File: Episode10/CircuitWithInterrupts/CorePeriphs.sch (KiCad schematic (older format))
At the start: 10 parts, among them J303 Conn_01x05, U301 82C55A, U302 82C54, U303 MC6850

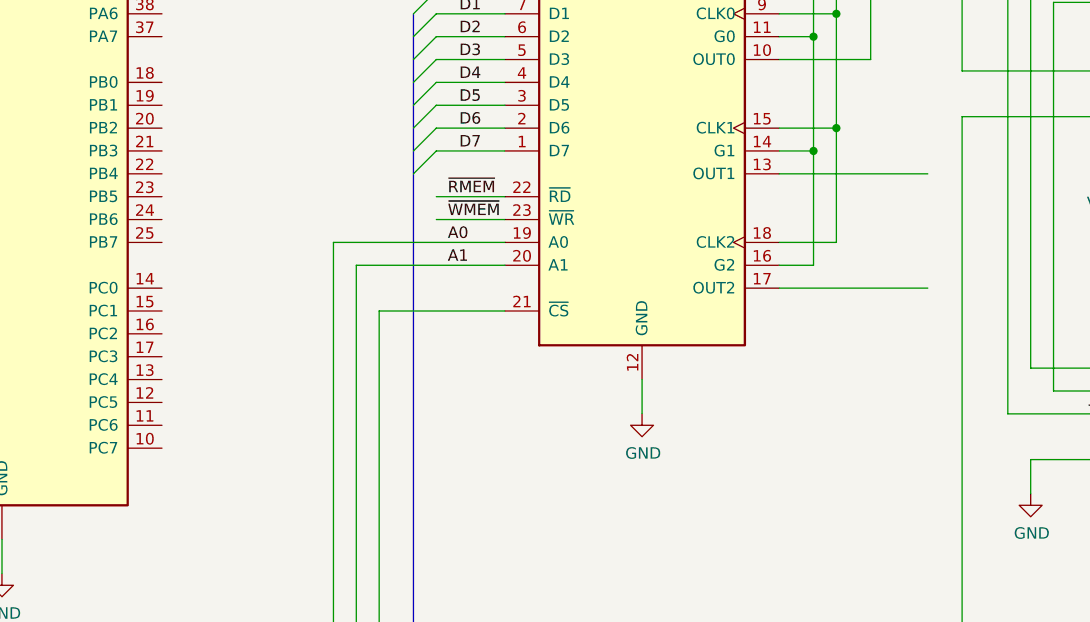
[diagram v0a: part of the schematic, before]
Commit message: integrated interrupt controller
Added ~IRQ input to core module, and changed the
wiring of the CPU's ~IRQ input to feed in the ~IRQ
output of the interrupt controller.  (A pull-up
resistor will keep this input high when the interrupt
controller isn't installed.)

Have the peripheral module send the Timer 1 output
to the interrupt controller's ~IRQ3 input.  This will
be the system periodic timer interrupt.

Also have the peripheral module export the pins of
Port C, and use PC0 and PC1 to clear the flip flops
that latch a pulse on ~IRQ3 and ~IRQ6, which are
edge-triggered.
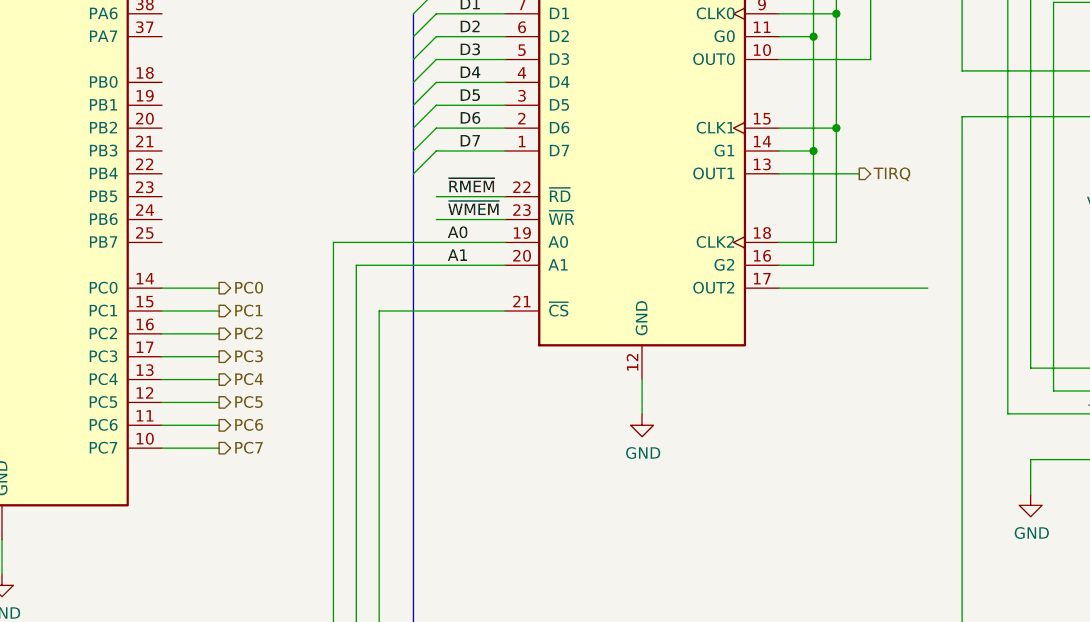
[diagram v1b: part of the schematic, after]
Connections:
- net PC7: now reaches U301.10 (PC7)
- net PC6: now reaches U301.11 (PC6)
- net PC5: now reaches U301.12 (PC5)
- net PC4: now reaches U301.13 (PC4)
- net PC0: now reaches U301.14 (PC0)
- net PC1: now reaches U301.15 (PC1)
- net PC2: now reaches U301.16 (PC2)
- net PC3: now reaches U301.17 (PC3)
- net TIRQ: now reaches U302.13 (OUT1)
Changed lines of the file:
@@
 	6600 2700 6600 2200
 Wire Wire Line
-	6350 2900 7000 2900
+	6350 2900 6700 2900
 Wire Wire Line
 	6350 3400 7000 3400
@@
 Wire Wire Line
 	7900 1900 7900 1950
+Text HLabel 6700 2900 2    50   Output ~ 0
+TIRQ
+Wire Wire Line
+	3650 3400 3900 3400
 Wire Bus Line
 	1950 5700 10300 5700
@@
 Wire Bus Line
 	1850 2900 1850 6650
+Wire Wire Line
+	3650 3500 3900 3500
+Wire Wire Line
+	3650 3600 3900 3600
+Wire Wire Line
+	3650 3700 3900 3700
+Wire Wire Line
+	3650 3800 3900 3800
+Wire Wire Line
+	3650 3900 3900 3900
+Wire Wire Line
+	3650 4000 3900 4000
+Wire Wire Line
+	3650 4100 3900 4100
+Text HLabel 3900 3400 2    50   Output ~ 0
+PC0
+Text HLabel 3900 3500 2    50   Output ~ 0
+PC1
+Text HLabel 3900 3600 2    50   Output ~ 0
+PC2
+Text HLabel 3900 3700 2    50   Output ~ 0
+PC3
+Text HLabel 3900 3800 2    50   Output ~ 0
+PC4
+Text HLabel 3900 3900 2    50   Output ~ 0
+PC5
+Text HLabel 3900 4000 2    50   Output ~ 0
+PC6
+Text HLabel 3900 4100 2    50   Output ~ 0
+PC7
 $EndSCHEMATC
